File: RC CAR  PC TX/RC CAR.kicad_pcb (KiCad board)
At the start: 2 copper layers, 29 parts, among them SW2 SW_SPST, SW3 SW_SPST, SW4 SW_SPST, SW5 SW_SPST, U1 Conn_02x07_Counter_Clockwise, U3 Pico, Y1 Crystal

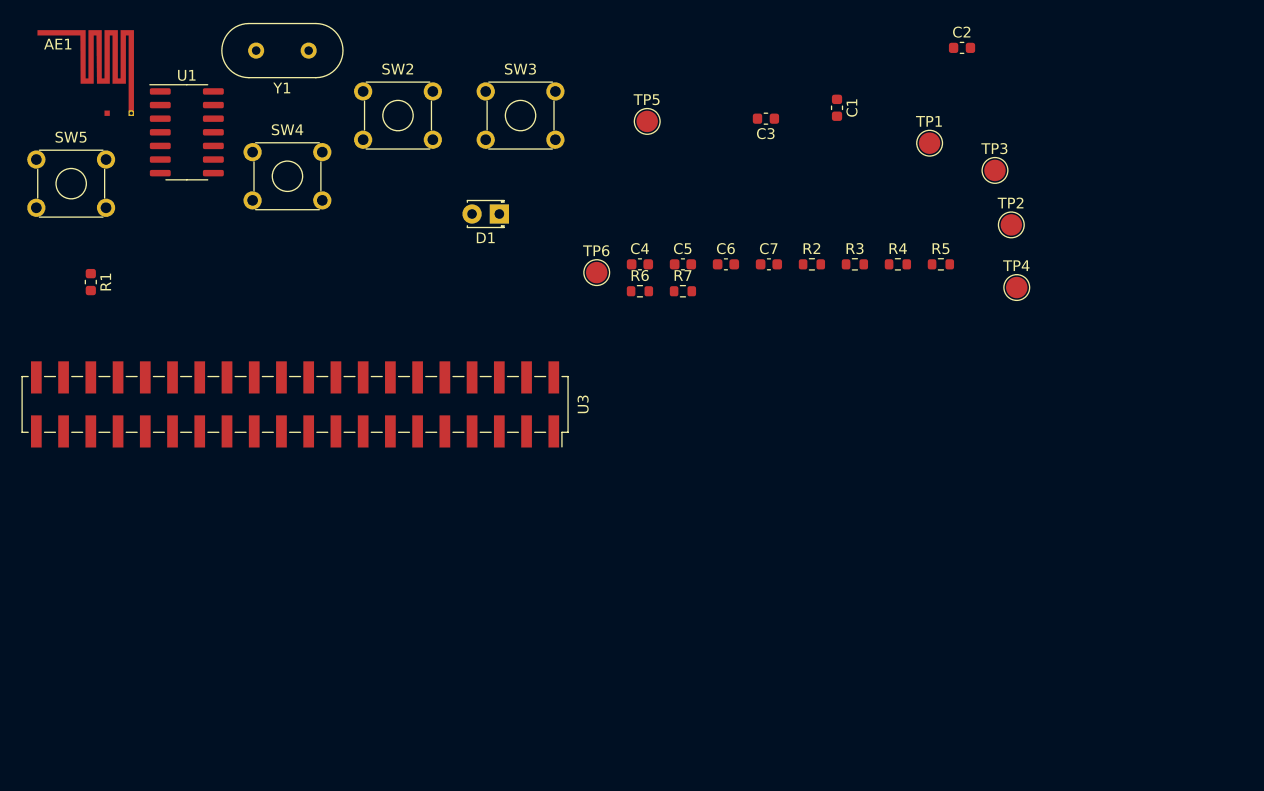
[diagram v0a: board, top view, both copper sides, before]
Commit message: Updated PCB layout for PCBA 2.0
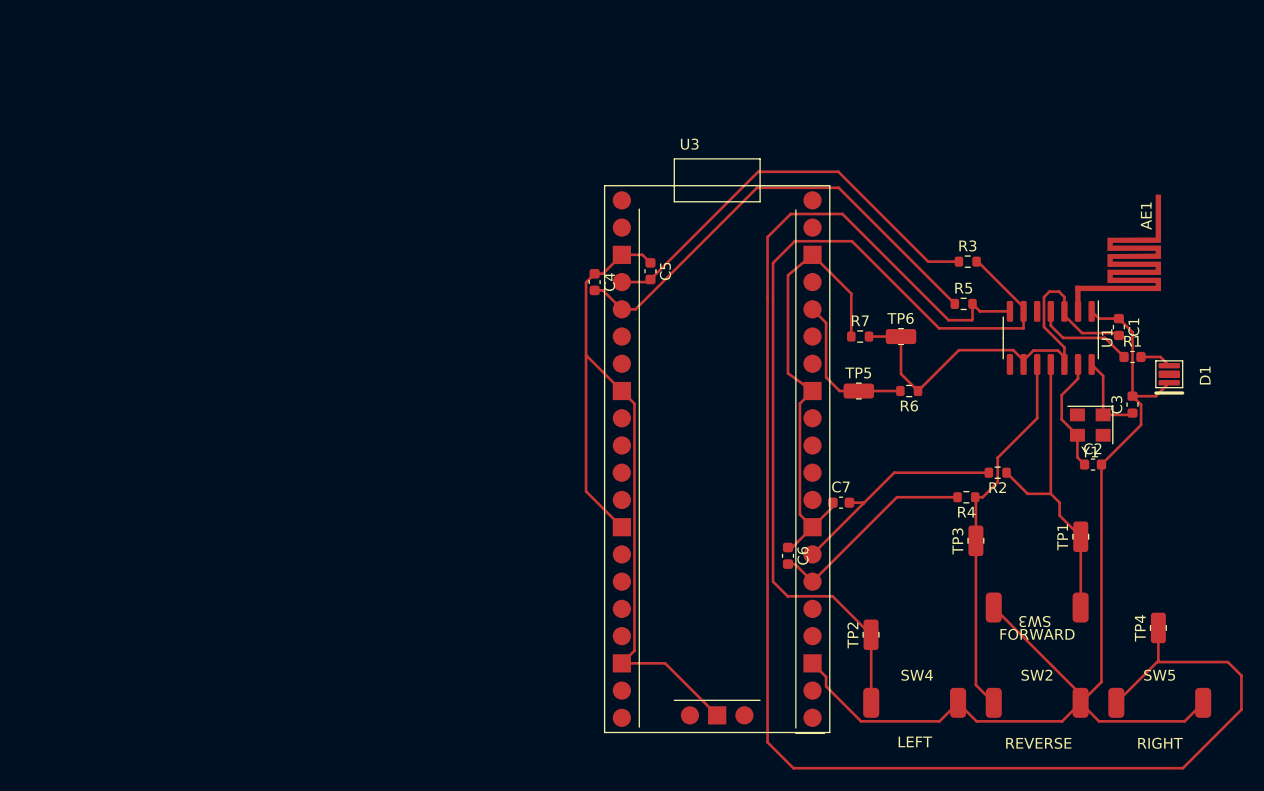
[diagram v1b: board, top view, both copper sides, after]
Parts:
- AE1: footprint RF_Antenna:SZJJX_CAR_TX_2.4GHz_Left -> RC_CAR_Library:SZJJX_CAR_TX_2.4GHz_Left
- C4, C5, C6, C7: value 20uF -> 22uF
- D1: footprint LED_THT:LED_D1.8mm_W3.3mm_H2.4mm -> RC_CAR_Library:DS144_Luxeon_LED_SMD_1CAT
- SW2: value SW_SPST -> SW_REVERSE; footprint Button_Switch_THT:SW_TH_Tactile_Omron_B3F-10xx -> RC CAR:RC TLS TacSwitch
- SW3: value SW_SPST -> SW_FORWARD; footprint Button_Switch_THT:SW_TH_Tactile_Omron_B3F-10xx -> RC CAR:RC TLS TacSwitch
- SW4: value SW_SPST -> SW_LEFT; footprint Button_Switch_THT:SW_TH_Tactile_Omron_B3F-10xx -> RC CAR:RC TLS TacSwitch
- SW5: value SW_SPST -> SW_RIGHT; footprint Button_Switch_THT:SW_TH_Tactile_Omron_B3F-10xx -> RC CAR:RC TLS TacSwitch
- TP1, TP2, TP3, TP4, TP5, TP6: footprint TestPoint:TestPoint_Pad_D2.0mm -> TestPoint:Test_Point_0805_2012Metric
- U3: footprint Connector_PinSocket_2.54mm:PinSocket_2x20_P2.54mm_Vertical_SMD -> RC_CAR_Library:Pico_Pi_Connector
- Y1: value Crystal -> Crystal_GND24; footprint Crystal:Crystal_HC18-U_Vertical -> Crystal:Crystal_SMD_SeikoEpson_FA238V-4Pin_3.2x2.5mm
- moved SW5 116.4 mm to (236.9, 114.2)
- moved R1 97.4 mm to (234.3, 81.9), turned to 0 degrees
- moved AE1 91.6 mm to (229.2, 73.3), turned to -90 degrees
- moved SW2 84.9 mm to (225.4, 114.2)
- moved U1 82.8 mm to (226.7, 80.1), turned to -90 degrees
- moved Y1 80.8 mm to (230.4, 88.3)
- moved SW4 80.3 mm to (214.0, 114.2)
- moved SW3 70.4 mm to (225.4, 105.3), turned to 180 degrees
- moved D1 64.2 mm to (237.7, 83.5), turned to 90 degrees
- moved C3 43.4 mm to (234.3, 86.4), turned to 90 degrees
- moved C2 40.7 mm to (230.6, 91.9)
- moved TP2 40.4 mm to (209.9, 107.8), turned to 90 degrees
- moved U3 39.7 mm to (195.6, 91.4), turned to 0 degrees
- moved TP1 39.3 mm to (229.5, 98.7), turned to 90 degrees
- moved TP3 34.6 mm to (219.7, 99.1), turned to 90 degrees
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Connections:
- C6 pad 2: Net-(C6-Pad2) -> Net-(U3-Pad26)
- C7 pad 2: Net-(C7-Pad2) -> Net-(U3-Pad27)
- R2 pad 1: Net-(C7-Pad2) -> /FORWARD
- R2 pad 2: /FORWARD -> Net-(U3-Pad27)
- R4 pad 1: Net-(C6-Pad2) -> /REVERSE
- R4 pad 2: /REVERSE -> Net-(U3-Pad26)
- U1 pad 5: Net-(U1-Pad5) -> unconnected-(U1-Pad5)
- U1 pad 8: Net-(U1-Pad8) -> unconnected-(U1-Pad8)
- U3 pad 1: Net-(C7-Pad2) -> unconnected-(U3-Pad1)
- U3 pad 10: Net-(U3-Pad10) -> unconnected-(U3-Pad10)
- U3 pad 11: Net-(U3-Pad11) -> unconnected-(U3-Pad11)
- U3 pad 12: Net-(U3-Pad12) -> unconnected-(U3-Pad12)
- U3 pad 14: Net-(U3-Pad14) -> unconnected-(U3-Pad14)
- U3 pad 15: Net-(U3-Pad15) -> unconnected-(U3-Pad15)
- U3 pad 16: Net-(U3-Pad16) -> unconnected-(U3-Pad16)
- U3 pad 17: Net-(U3-Pad17) -> unconnected-(U3-Pad17)
- U3 pad 19: Net-(U3-Pad19) -> unconnected-(U3-Pad19)
- U3 pad 2: Net-(C6-Pad2) -> unconnected-(U3-Pad2)
- U3 pad 20: Net-(U3-Pad20) -> unconnected-(U3-Pad20)
- U3 pad 21: Net-(U3-Pad21) -> unconnected-(U3-Pad21)
- U3 pad 22: Net-(U3-Pad22) -> unconnected-(U3-Pad22)
- U3 pad 24: Net-(U3-Pad24) -> unconnected-(U3-Pad24)
- U3 pad 25: Net-(U3-Pad25) -> unconnected-(U3-Pad25)
- U3 pad 29: Net-(U3-Pad29) -> unconnected-(U3-Pad29)
- U3 pad 30: Net-(U3-Pad30) -> unconnected-(U3-Pad30)
- U3 pad 31: Net-(U3-Pad31) -> unconnected-(U3-Pad31)
- U3 pad 32: Net-(U3-Pad32) -> unconnected-(U3-Pad32)
- U3 pad 34: Net-(U3-Pad34) -> unconnected-(U3-Pad34)
- U3 pad 35: Net-(U3-Pad35) -> unconnected-(U3-Pad35)
- U3 pad 37: Net-(U3-Pad37) -> unconnected-(U3-Pad37)
- U3 pad 39: Net-(U3-Pad39) -> unconnected-(U3-Pad39)
- U3 pad 40: Net-(U3-Pad40) -> unconnected-(U3-Pad40)
- U3 pad 6: Net-(U3-Pad6) -> unconnected-(U3-Pad6)
- U3 pad 7: Net-(U3-Pad7) -> unconnected-(U3-Pad7)
- U3 pad 9: Net-(U3-Pad9) -> unconnected-(U3-Pad9)
- Y1 pad 1: Net-(C2-Pad1) -> Net-(C3-Pad1)
- Y1 pad 2: Net-(C3-Pad1) -> unconnected-(Y1-Pad2)
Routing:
- net GND: track 0.00 -> 218.7 mm
- net /RIGHT: track 0.00 -> 144.3 mm
- net /LEFT: track 0.00 -> 83.0 mm
- net Net-(C4-Pad2): track 0.00 -> 43.5 mm
- net +3V0: track 0.00 -> 43.0 mm
- net Net-(C5-Pad2): track 0.00 -> 39.2 mm
- net /REVERSE: track 0.00 -> 35.0 mm
- net /FORWARD: track 0.00 -> 28.8 mm
- net Net-(U3-Pad27): track 0.00 -> 21.0 mm
- net Net-(U3-Pad26): track 0.00 -> 19.8 mm
- net +3V3: track 0.00 -> 14.3 mm
- net Net-(C2-Pad1): track 0.00 -> 10.9 mm
- net Net-(R1-Pad1): track 0.00 -> 9.37 mm
- net Net-(C3-Pad1): track 0.00 -> 7.90 mm
- net Net-(D1-Pad2): track 0.00 -> 2.98 mm
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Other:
- net class Default removed
- board text added: "FORWARD"
- board text added: "LEFT"
- board text added: "REVERSE"
- board text added: "RIGHT"

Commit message: Updated files
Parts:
- SW2, SW3, SW4, SW5: footprint RC CAR:RC TLS TacSwitch -> RC_CAR_Library:RC TLS TacSwitch
- TP1, TP2, TP3, TP4, TP5, TP6: footprint TestPoint:Test_Point_0805_2012Metric -> RC_CAR_Library:Test_Point_0805_2012Metric
- U1: value Conn_02x07_Counter_Clockwise -> RC_PCBA_TX
- moved TP2 8.00 mm to (217.9, 107.8)
- moved TP5 3.02 mm to (209.9, 87.9)
- moved C7 2.54 mm to (209.0, 97.2), turned to -90 degrees
- moved C4 2.29 mm to (181.9, 75.1)
- moved C6 2.16 mm to (200.0, 100.3)
- moved C5 1.80 mm to (191.1, 73.7)
- moved R7 1.07 mm to (209.6, 80.8), turned to 90 degrees
- moved AE1 0.12 mm to (229.2, 73.2)
- moved TP6 0.06 mm to (212.7, 80.0)
- turned SW4 to 180 degrees
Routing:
- net GND: track 218.7 -> 200.3 mm
- net +3V3: track 14.3 -> 21.4 mm
- net /RIGHT: track 144.3 -> 137.7 mm
- net /LEFT: track 83.0 -> 86.7 mm
- net Net-(U3-Pad27): track 21.0 -> 17.9 mm
- net Net-(C4-Pad2): track 43.5 -> 45.8 mm
- net Net-(U3-Pad26): track 19.8 -> 22.0 mm
- net Net-(C5-Pad2): track 39.2 -> 38.4 mm
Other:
- board outline added: 64.2 x 55.9 mm
- board text added: "3V0"
- board text added: "3V3"
- board text added: "LED"
